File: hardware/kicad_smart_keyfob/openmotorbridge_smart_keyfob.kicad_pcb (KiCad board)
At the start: 2 copper layers, 38 x 19 mm, 25 parts, among them M1 LRA_MOTOR_PADS, SW1 BTN_ARM, SW2 BTN_SOS, U1 nRF52840-QIAA, U2 SX1262IMLTRT, U3 DRV2605LDGSR, U4 BQ51003YFPR, U5 BQ25100YFPR, Y1 32.000MHz, Y2 32.768kHz, Y3 32MHz_TCXO

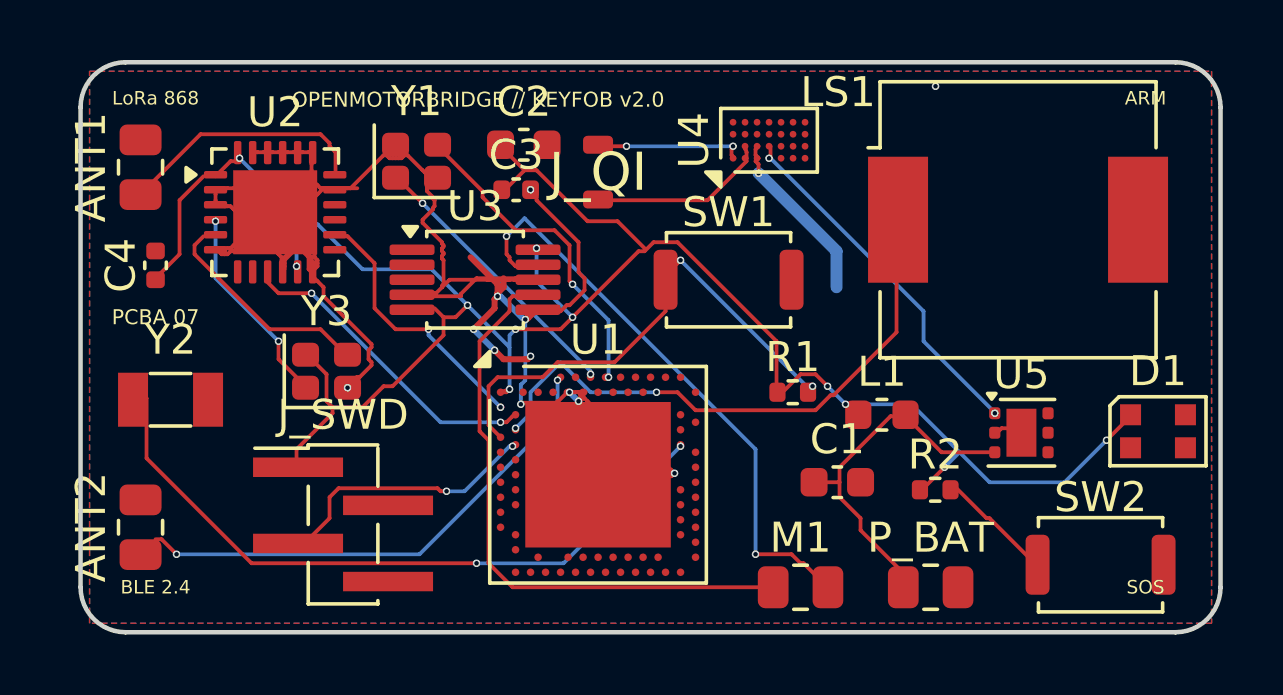
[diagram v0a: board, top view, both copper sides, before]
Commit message: feat(hw): finalize PCB lineup routing, sync PCBA 03 cartridge with J_PROG header and DTM12 schematics
- PCBA 01 (Central Box): Remediate net routing, DTM12 hierarchical schematic synchronization, 100% routed, 0 DRC errors.
- PCBA 03 (Smart Modular Cartridge): Position and route J_PROG 4-pin SMD programming header on F.Cu at (108.0, 89.61), synchronize CPL and schematic, 100% routed, 0 DRC errors.
- PCBA 05 (Universal Front Node): Preconnect and routing verified, 100% routed, 0 DRC errors.
- PCBA 07 (LoRa Smart-Keyfob): Routing and DRC verified, 100% routed, 0 DRC errors.
- PCBA 08 (Radar 2.0 Sub-MCU & Wings): Sub-MCU routing and HF isolation verified, 100% routed, 0 DRC errors.
- PCBA 10 (OMM 446 PMR/DMR Intercom): KiCad DRC verified, 100% routed, 0 DRC errors.
- Firmware: Align configuration headers across front_node and smart_cartridge.
- Tools: Add comprehensive preflight PCBA audit suite tools/audit_pcbas_preflight.py.
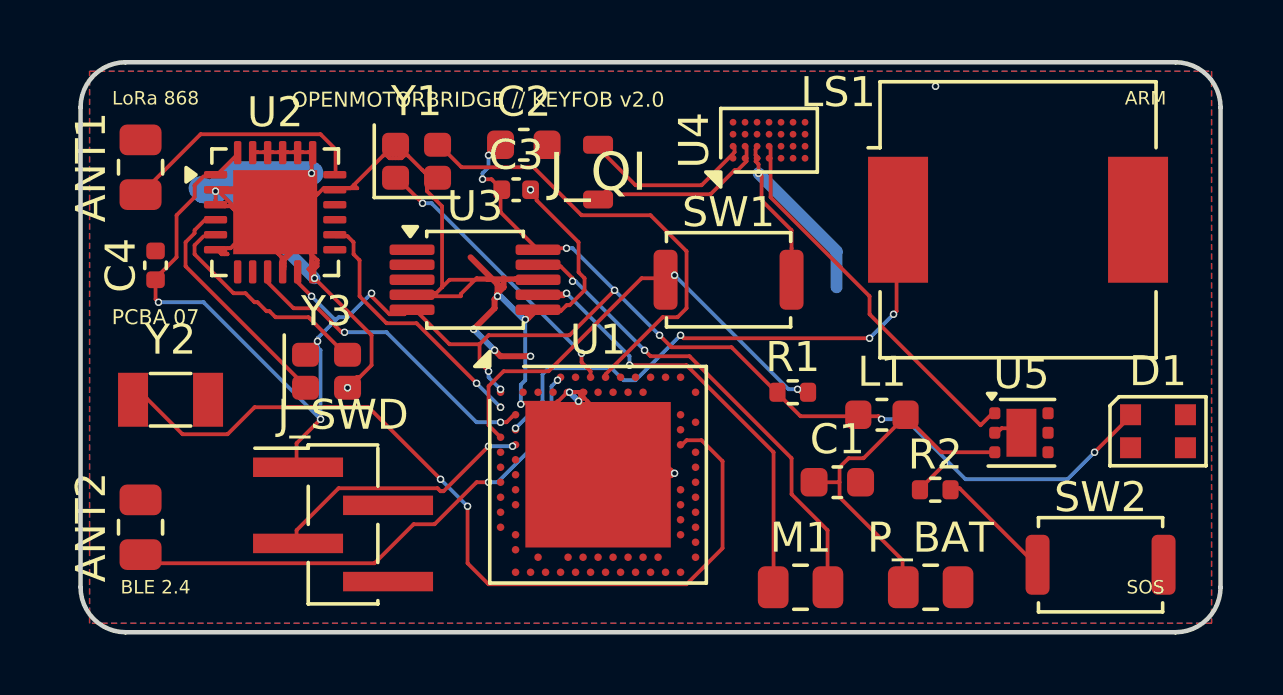
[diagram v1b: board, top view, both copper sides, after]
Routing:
- net GND: track 59.8 -> 73.1 mm, vias 13 -> 16
- net VCC_3V3: track 71.3 -> 63.3 mm, vias 11 -> 15
- net RTC2: track 23.3 -> 29.2 mm
- net LRA_POS: track 20.1 -> 15.8 mm, vias 0 -> 2
- net XTAL2: track 10.9 -> 15.3 mm, vias 2 -> 0
- net LRA_NEG: track 19.9 -> 16.0 mm
- net BTN_ARM_N: track 16.7 -> 15.3 mm
- net TCXO_IN: track 6.74 -> 7.55 mm, vias 2 -> 0
- net VCC_QI_5V: track 12.0 -> 12.8 mm, vias 2 -> 0
- net QI_AC1: track 5.08 -> 5.79 mm, vias 2 -> 0
- net BUZZER_PWM: track 18.5 -> 18.4 mm, vias 2 -> 4
